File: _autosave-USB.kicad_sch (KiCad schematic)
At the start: 7 parts

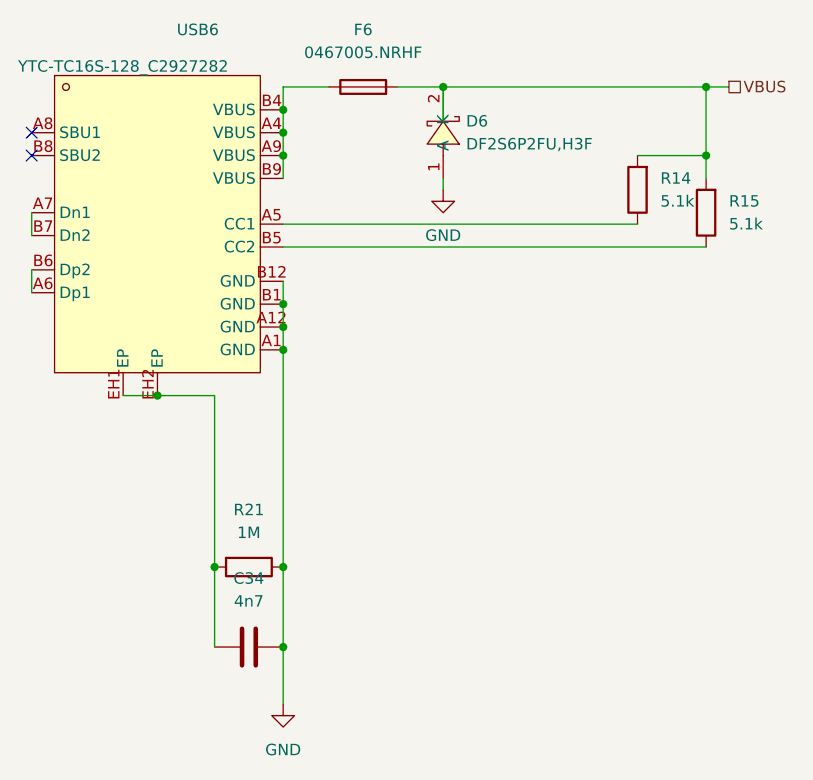
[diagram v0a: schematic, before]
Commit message: finished getting footprints and started layout
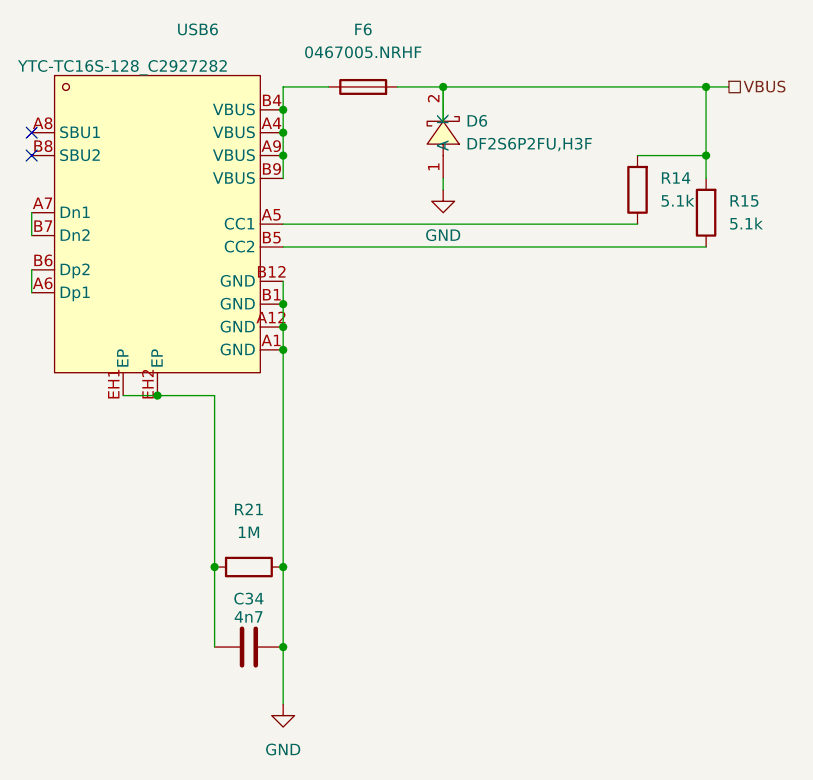
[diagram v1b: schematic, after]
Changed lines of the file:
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@@
 		(on_board yes)
 		(dnp no)
-		(fields_autoplaced yes)
 		(property "Reference" "C34"
-			(at 142.24 111.76 90)
+			(at 142.24 114.046 90)
 			(effects
 				(font
@@
 		)
 		(property "Value" "4n7"
-			(at 142.24 114.3 90)
+			(at 142.24 116.078 90)
 			(effects
 				(font
